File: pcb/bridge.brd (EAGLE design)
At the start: 102.5 x 66 mm, 31 parts, among them IC1 ARDUINO_PRO_MICRO, IC2 LM358D, X1 SZARKBUS, X2 RSENSE, X3 +12V

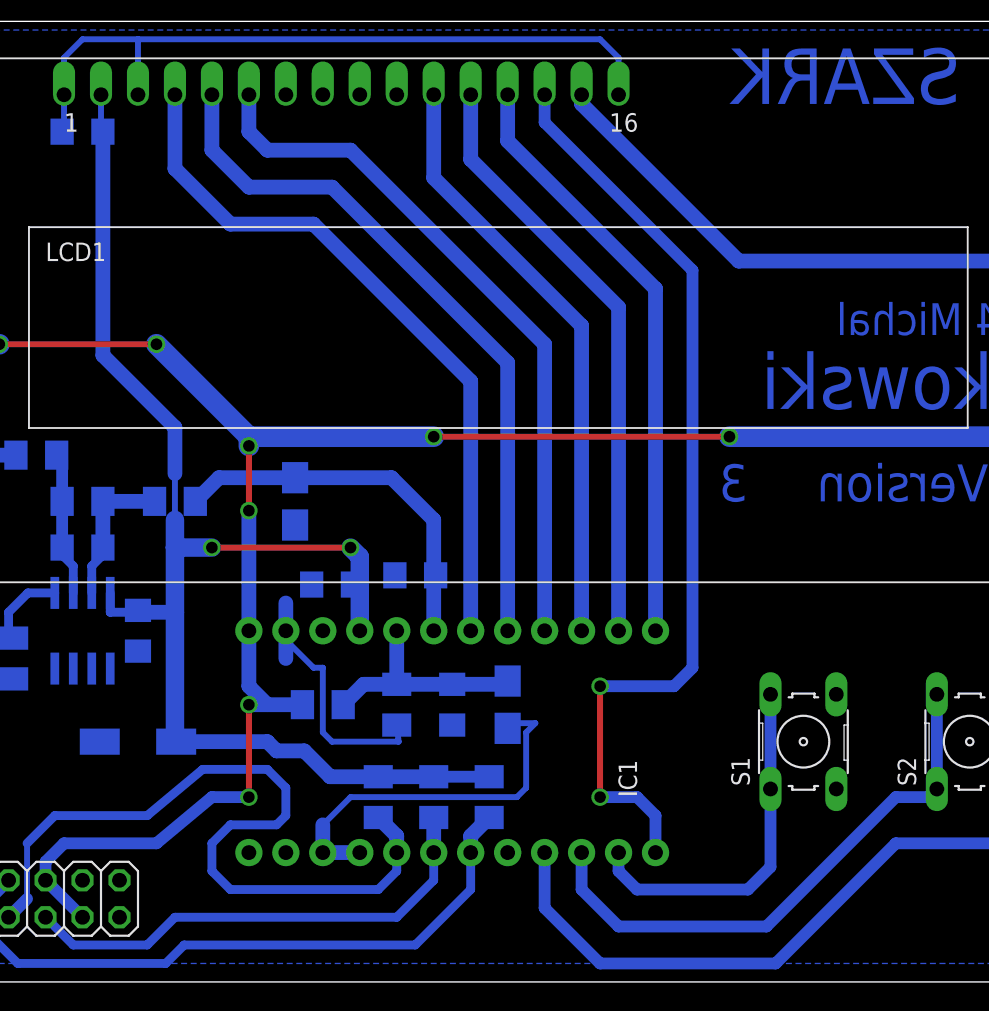
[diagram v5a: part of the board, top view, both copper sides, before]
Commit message: bridge: Connect unused op-amp to the ground.
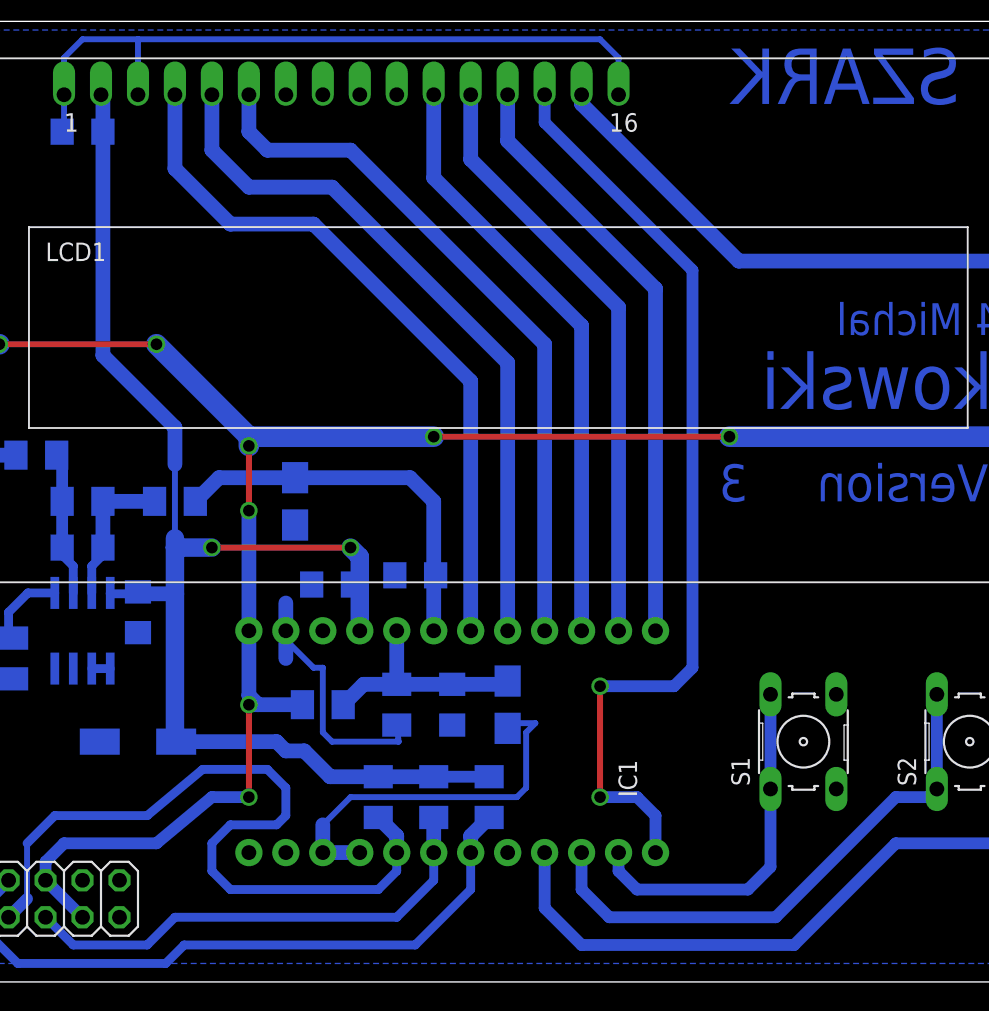
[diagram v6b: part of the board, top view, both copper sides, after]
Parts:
- moved C9 1.27 mm to (26.7, 25.4)
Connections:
- removed net RX: IC1.2
- removed net TX: IC1.1
- new net N$12: IC2.1, IC2.2
- net GND: now also IC2.3
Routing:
- net +5V: track 93.7 -> 92.4 mm
- net N$12: track 0.00 -> 1.27 mm
- net BTN1: track 55.2 -> 54.2 mm
- net ACURR: track 26.0 -> 26.7 mm
- net BTN2: track 38.4 -> 37.9 mm
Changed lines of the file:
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@@
 <circle x="97" y="60" radius="5" width="0" layer="42"/>
 <dimension x1="0" y1="0" x2="102.5" y2="0" x3="51.25" y3="-9.5" textsize="1.778" layer="20" dtype="horizontal"/>
-<dimension x1="0" y1="0" x2="30.48" y2="20.32" x3="15.24" y3="-13.97" textsize="1.778" layer="20" dtype="horizontal"/>
 <circle x="13.97" y="60.96" radius="4.5" width="0" layer="42"/>
 <circle x="88.9" y="60.96" radius="4.5" width="0" layer="42"/>
@@
 <text x="97.155" y="39.37" size="3.81" layer="16" font="vector" rot="MR0">Slomkowski</text>
 <text x="95.885" y="44.45" size="2.1844" layer="16" font="vector" rot="MR0">(C) 2014 Michal</text>
+<rectangle x1="65.405" y1="32.385" x2="97.155" y2="48.26" layer="30"/>
 </plain>
 <attributes>
@@
 <element name="C11" library="rcl" package="C1206" value="100n" x="22.86" y="58.42" rot="MR0"/>
 <element name="C8" library="rcl" package="C/6032-28W" value="47u" x="26.67" y="16.51" rot="MR180"/>
-<element name="C9" library="rcl" package="C1206" value="100n" x="26.67" y="24.13" rot="MR270"/>
+<element name="C9" library="rcl" package="C1206" value="100n" x="26.67" y="25.4" rot="MR270"/>
 <element name="C7" library="rcl" package="C1206" value="100n" x="40.005" y="27.305" rot="MR0"/>
 </elements>
@@
 <wire x1="21.59" y1="58.55" x2="21.46" y2="58.42" width="0.4064" layer="16"/>
 <wire x1="15.24" y1="6.985" x2="15.24" y2="4.445" width="0.8128" layer="16"/>
-<polygon width="0.3048" layer="16" isolate="1.016">
+<polygon width="0.4064" layer="16" isolate="1.016">
 <vertex x="1.27" y="65.405"/>
 <vertex x="1.27" y="1.27"/>
@@
 <wire x1="39.37" y1="8.89" x2="39.37" y2="10.795" width="1.016" layer="16"/>
 <wire x1="36.83" y1="26.035" x2="36.83" y2="22.225" width="1.016" layer="16"/>
+<contactref element="IC2" pad="3"/>
+<wire x1="20.955" y1="21.53" x2="22.225" y2="21.53" width="0" layer="19" extent="16-16"/>
 </signal>
 <signal name="+5V">
@@
 <contactref element="IC2" pad="8"/>
 <contactref element="C9" pad="1"/>
-<wire x1="24.13" y1="60.96" x2="24.13" y2="58.55" width="0.4064" layer="16"/>
-<wire x1="24.13" y1="58.55" x2="24.26" y2="58.42" width="0.4064" layer="16"/>
 <wire x1="24.26" y1="58.42" x2="24.13" y2="58.42" width="0.4064" layer="16"/>
 <wire x1="46.99" y1="14.1" x2="50.8" y2="14.1" width="0.8128" layer="16"/>
 <wire x1="43.18" y1="14.1" x2="39.875" y2="14.1" width="1.016" layer="16"/>
 <wire x1="39.875" y1="14.1" x2="38.1" y2="15.875" width="1.016" layer="16"/>
-<wire x1="38.1" y1="15.875" x2="36.195" y2="15.875" width="1.016" layer="16"/>
-<wire x1="36.195" y1="15.875" x2="35.56" y2="16.51" width="1.016" layer="16"/>
+<wire x1="38.1" y1="15.875" x2="36.83" y2="15.875" width="1.016" layer="16"/>
+<wire x1="36.83" y1="15.875" x2="36.195" y2="16.51" width="1.016" layer="16"/>
 <wire x1="43.18" y1="14.1" x2="46.99" y2="14.1" width="1.016" layer="16"/>
-<wire x1="35.56" y1="16.51" x2="29.295" y2="16.51" width="1.016" layer="16"/>
+<wire x1="36.195" y1="16.51" x2="29.295" y2="16.51" width="1.016" layer="16"/>
 <via x="31.75" y="29.845" extent="1-16" drill="0.8" shape="octagon"/>
 <wire x1="31.75" y1="29.845" x2="41.275" y2="29.845" width="0.4064" layer="1"/>
@@
 <wire x1="41.91" y1="29.21" x2="41.91" y2="27.305" width="1.27" layer="16"/>
 <wire x1="41.91" y1="27.305" x2="41.91" y2="24.13" width="1.27" layer="16"/>
-<wire x1="26.67" y1="25.53" x2="26.54" y2="25.4" width="0.6096" layer="16"/>
-<wire x1="26.54" y1="25.4" x2="24.765" y2="25.4" width="0.6096" layer="16"/>
-<wire x1="24.765" y1="25.4" x2="24.765" y2="26.73" width="0.6096" layer="16"/>
-<wire x1="26.67" y1="25.53" x2="26.8" y2="25.4" width="1.016" layer="16"/>
+<wire x1="26.67" y1="26.8" x2="26.54" y2="26.67" width="0.6096" layer="16"/>
+<wire x1="26.54" y1="26.67" x2="24.765" y2="26.67" width="0.6096" layer="16"/>
+<wire x1="24.765" y1="26.67" x2="24.765" y2="26.73" width="0.6096" layer="16"/>
+<wire x1="26.67" y1="26.8" x2="26.8" y2="26.67" width="1.016" layer="16"/>
 <wire x1="24.26" y1="58.42" x2="24.26" y2="43.05" width="1.016" layer="16"/>
 <wire x1="24.26" y1="43.05" x2="29.21" y2="38.1" width="1.016" layer="16"/>
-<wire x1="29.21" y1="38.1" x2="29.21" y2="34.925" width="1.016" layer="16"/>
-<wire x1="29.21" y1="34.925" x2="29.21" y2="31.75" width="0.4064" layer="16"/>
-<wire x1="29.21" y1="31.75" x2="29.21" y2="29.845" width="1.27" layer="16"/>
-<wire x1="29.21" y1="29.845" x2="29.21" y2="25.4" width="1.27" layer="16"/>
-<wire x1="29.21" y1="25.4" x2="29.21" y2="16.595" width="1.27" layer="16"/>
+<wire x1="29.21" y1="38.1" x2="29.21" y2="35.56" width="1.016" layer="16"/>
+<wire x1="29.21" y1="35.56" x2="29.21" y2="30.48" width="0.4064" layer="16"/>
+<wire x1="29.21" y1="30.48" x2="29.21" y2="29.845" width="1.27" layer="16"/>
+<wire x1="29.21" y1="29.845" x2="29.21" y2="26.67" width="1.27" layer="16"/>
+<wire x1="29.21" y1="26.67" x2="29.21" y2="16.595" width="1.27" layer="16"/>
 <wire x1="29.21" y1="16.595" x2="29.295" y2="16.51" width="1.27" layer="16"/>
 <wire x1="31.75" y1="29.845" x2="29.21" y2="29.845" width="1.27" layer="16"/>
-<wire x1="26.8" y1="25.4" x2="29.21" y2="25.4" width="1.016" layer="16"/>
+<wire x1="26.8" y1="26.67" x2="29.21" y2="26.67" width="1.016" layer="16"/>
 <contactref element="C7" pad="1"/>
 <wire x1="41.405" y1="27.305" x2="41.91" y2="27.305" width="1.016" layer="16"/>
+<wire x1="24.26" y1="58.42" x2="24.26" y2="60.83" width="1.016" layer="16"/>
+<wire x1="24.26" y1="60.83" x2="24.13" y2="60.96" width="1.016" layer="16"/>
 </signal>
 <signal name="+12V">
@@
 <contactref element="X1" pad="6"/>
 <wire x1="20.32" y1="6.985" x2="22.86" y2="4.445" width="0.8128" layer="16"/>
-<wire x1="34.29" y1="24.13" x2="34.29" y2="20.32" width="1.016" layer="16"/>
-<wire x1="34.29" y1="20.32" x2="35.56" y2="19.05" width="1.016" layer="16"/>
-<wire x1="35.56" y1="19.05" x2="34.29" y2="19.05" width="1.016" layer="16"/>
+<wire x1="34.29" y1="24.13" x2="34.29" y2="19.685" width="1.016" layer="16"/>
+<wire x1="34.29" y1="19.685" x2="34.925" y2="19.05" width="1.016" layer="16"/>
+<wire x1="34.925" y1="19.05" x2="34.29" y2="19.05" width="1.016" layer="16"/>
 <via x="34.29" y="19.05" extent="1-16" drill="0.8" shape="octagon"/>
 <wire x1="34.29" y1="19.05" x2="34.29" y2="12.7" width="0.4064" layer="1"/>
@@
 <wire x1="21.59" y1="9.525" x2="20.32" y2="8.255" width="0.8128" layer="16"/>
 <wire x1="20.32" y1="8.255" x2="20.32" y2="6.985" width="0.8128" layer="16"/>
-<wire x1="35.56" y1="19.05" x2="37.97" y2="19.05" width="1.016" layer="16"/>
+<wire x1="34.925" y1="19.05" x2="37.97" y2="19.05" width="1.016" layer="16"/>
 <wire x1="6.45" y1="47.78" x2="6.45" y2="43.28" width="1.4224" layer="16"/>
 <wire x1="6.45" y1="43.28" x2="5.715" y2="41.91" width="1.4224" layer="16"/>
@@
 <wire x1="46.99" y1="24.13" x2="46.99" y2="27.81" width="1.016" layer="16"/>
 <wire x1="46.99" y1="27.81" x2="47.12" y2="27.94" width="1.016" layer="16"/>
-<wire x1="37.465" y1="34.645" x2="44.095" y2="34.645" width="1.016" layer="16"/>
-<wire x1="44.095" y1="34.645" x2="46.99" y2="31.75" width="1.016" layer="16"/>
-<wire x1="46.99" y1="31.75" x2="46.99" y2="28.07" width="1.016" layer="16"/>
+<wire x1="37.465" y1="34.645" x2="45.365" y2="34.645" width="1.016" layer="16"/>
+<wire x1="45.365" y1="34.645" x2="46.99" y2="33.02" width="1.016" layer="16"/>
+<wire x1="46.99" y1="33.02" x2="46.99" y2="28.07" width="1.016" layer="16"/>
 <wire x1="46.99" y1="28.07" x2="47.12" y2="27.94" width="1.016" layer="16"/>
 <wire x1="37.465" y1="34.645" x2="32.235" y2="34.645" width="1.016" layer="16"/>
@@
 <wire x1="6.45" y1="27.46" x2="6.45" y2="25.17" width="1.016" layer="16"/>
 <wire x1="6.45" y1="25.17" x2="8.125" y2="23.495" width="1.016" layer="16"/>
-</signal>
-<signal name="RX">
-<contactref element="IC1" pad="2"/>
 </signal>
 <signal name="SDA">
@@
 <wire x1="31.75" y1="57.15" x2="31.75" y2="60.96" width="1.016" layer="16"/>
 </signal>
-<signal name="TX">
-<contactref element="IC1" pad="1"/>
-</signal>
 <signal name="BTN3">
 <contactref element="IC1" pad="11"/>
@@
 <contactref element="S3" pad="2"/>
 <wire x1="54.61" y1="8.89" x2="54.61" y2="5.08" width="0.8128" layer="16"/>
-<wire x1="54.61" y1="5.08" x2="58.42" y2="1.27" width="0.8128" layer="16"/>
-<wire x1="58.42" y1="1.27" x2="70.485" y2="1.27" width="0.8128" layer="16"/>
-<wire x1="70.485" y1="1.27" x2="78.74" y2="9.525" width="0.8128" layer="16"/>
+<wire x1="54.61" y1="5.08" x2="57.15" y2="2.54" width="0.8128" layer="16"/>
+<wire x1="57.15" y1="2.54" x2="71.755" y2="2.54" width="0.8128" layer="16"/>
+<wire x1="71.755" y1="2.54" x2="78.74" y2="9.525" width="0.8128" layer="16"/>
 <wire x1="78.74" y1="9.525" x2="89.2556" y2="9.525" width="0.8128" layer="16"/>
 <wire x1="89.2556" y1="9.525" x2="92.9894" y2="13.2588" width="0.8128" layer="16"/>
@@
 <wire x1="81.5594" y1="19.7612" x2="81.5594" y2="13.2588" width="0.8128" layer="16"/>
 <wire x1="57.15" y1="8.89" x2="57.15" y2="6.35" width="0.8128" layer="16"/>
-<wire x1="57.15" y1="6.35" x2="59.69" y2="3.81" width="0.8128" layer="16"/>
-<wire x1="59.69" y1="3.81" x2="69.85" y2="3.81" width="0.8128" layer="16"/>
-<wire x1="69.85" y1="3.81" x2="78.74" y2="12.7" width="0.8128" layer="16"/>
+<wire x1="57.15" y1="6.35" x2="59.055" y2="4.445" width="0.8128" layer="16"/>
+<wire x1="59.055" y1="4.445" x2="70.485" y2="4.445" width="0.8128" layer="16"/>
+<wire x1="70.485" y1="4.445" x2="78.74" y2="12.7" width="0.8128" layer="16"/>
 <wire x1="78.74" y1="12.7" x2="81.0006" y2="12.7" width="0.8128" layer="16"/>
 <wire x1="81.0006" y1="12.7" x2="81.5594" y2="13.2588" width="0.8128" layer="16"/>
@@
 <via x="88.9" y="60.96" extent="1-16" drill="1"/>
 </signal>
+<signal name="N$12">
+<contactref element="IC2" pad="1"/>
+<contactref element="IC2" pad="2"/>
+<wire x1="24.765" y1="21.53" x2="23.495" y2="21.53" width="0.6096" layer="16"/>
+</signal>
 </signals>
+<errors>
+</errors>
 </board>
 </drawing>

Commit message: bridge: Update resistor values.
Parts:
- C1, C5: value 4u7 -> 22u
- R2: value 470 -> 1k
- R6, R7: value 8k2 -> 4k7
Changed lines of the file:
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@@
 <element name="C10" library="rcl" package="E5-8,5" value="470u" x="5.715" y="39.37" rot="R270"/>
 <element name="IC2" library="linear" package="SO08" value="LM358D" x="22.86" y="24.13" rot="MR0"/>
-<element name="R6" library="rcl" package="M1206" value="8k2" x="9.525" y="23.495" rot="MR180"/>
-<element name="R7" library="rcl" package="M1206" value="8k2" x="19.685" y="36.195" rot="MR180"/>
+<element name="R6" library="rcl" package="M1206" value="4k7" x="9.525" y="23.495" rot="MR180"/>
+<element name="R7" library="rcl" package="M1206" value="4k7" x="19.685" y="36.195" rot="MR180"/>
 <element name="R8" library="rcl" package="M1206" value="10k" x="13.97" y="22.225" rot="MR90"/>
 <element name="R9" library="rcl" package="M1206" value="10k" x="22.86" y="33.02" rot="MR180"/>
@@
 <element name="R10" library="rcl" package="M1206" value="1k" x="29.21" y="33.02" rot="MR180"/>
 <element name="R1" library="rcl" package="M1206" value="8k2" x="39.37" y="19.05" rot="MR0"/>
-<element name="R2" library="rcl" package="M1206" value="470" x="44.45" y="19.05" rot="MR90"/>
+<element name="R2" library="rcl" package="M1206" value="1k" x="44.45" y="19.05" rot="MR90"/>
 <element name="C4" library="rcl" package="C1206" value="100n" x="22.86" y="29.845" rot="MR0"/>
 <element name="R11" library="rcl" package="0207/12" value="680" x="95.885" y="43.18" rot="R270"/>
 <element name="C2" library="rcl" package="C1206" value="100n" x="48.26" y="19.05" rot="MR270"/>
 <element name="IC1" library="sparkfun-boards" package="ARDUINO_PRO_MICRO" value="ARDUINO_PRO_MICRO" x="46.99" y="16.51" rot="R90"/>
-<element name="C1" library="rcl" package="B/3528-21W" value="4u7" x="52.07" y="19.05" rot="MR90"/>
-<element name="C5" library="rcl" package="B/3528-21W" value="4u7" x="37.465" y="33.02" rot="MR90"/>
+<element name="C1" library="rcl" package="B/3528-21W" value="22u" x="52.07" y="19.05" rot="MR90"/>
+<element name="C5" library="rcl" package="B/3528-21W" value="22u" x="37.465" y="33.02" rot="MR90"/>
 <element name="C6" library="rcl" package="C1206" value="100n" x="45.72" y="27.94" rot="MR0"/>
 <element name="X2" library="con-phoenix-350" package="1751248" value="RSENSE" x="6.35" y="29.21" rot="R90">
@@
 <wire x1="36.83" y1="26.035" x2="36.83" y2="22.225" width="1.016" layer="16"/>
 <contactref element="IC2" pad="3"/>
-<wire x1="20.955" y1="21.53" x2="22.225" y2="21.53" width="0" layer="19" extent="16-16"/>
 </signal>
 <signal name="+5V">
